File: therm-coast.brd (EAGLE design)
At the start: 44.1 x 36.8 mm, 19 parts, among them U1 ATTINY85-20SU

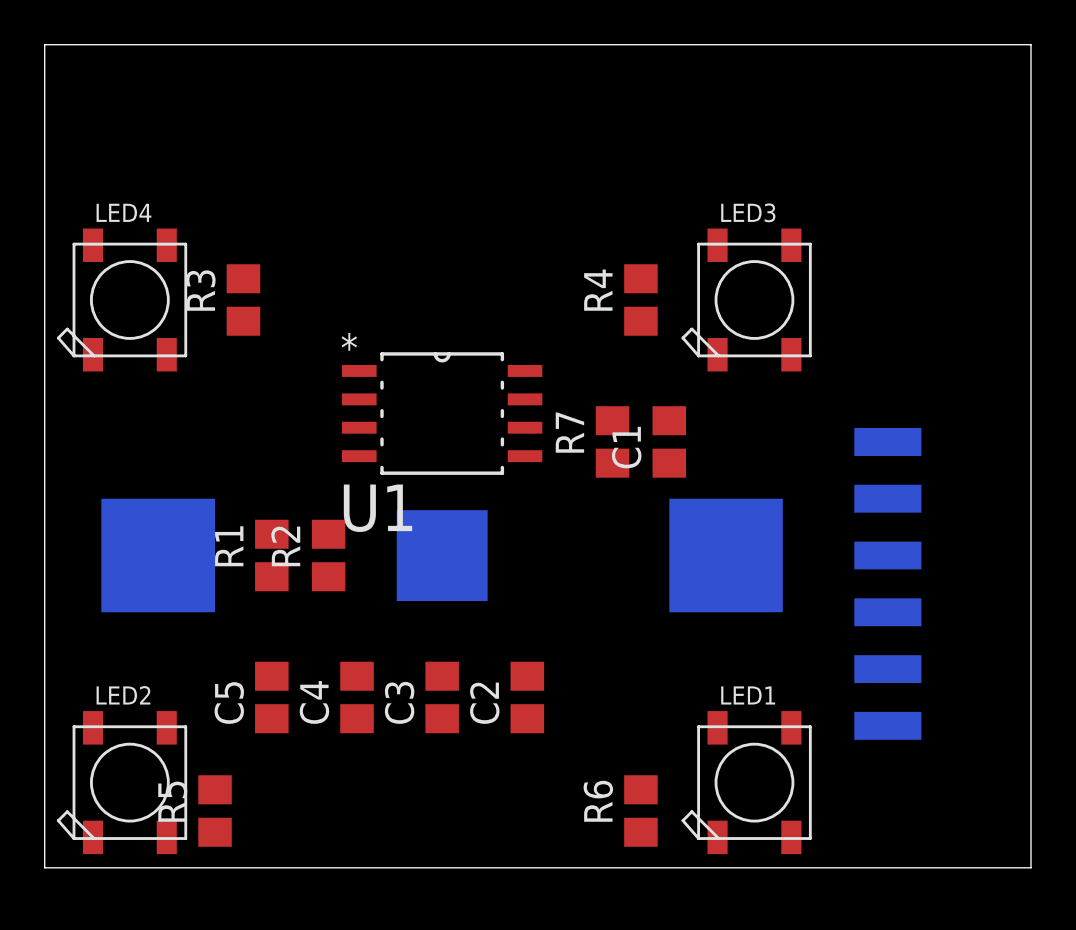
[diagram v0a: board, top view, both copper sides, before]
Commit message: Board Placement and Routing updates
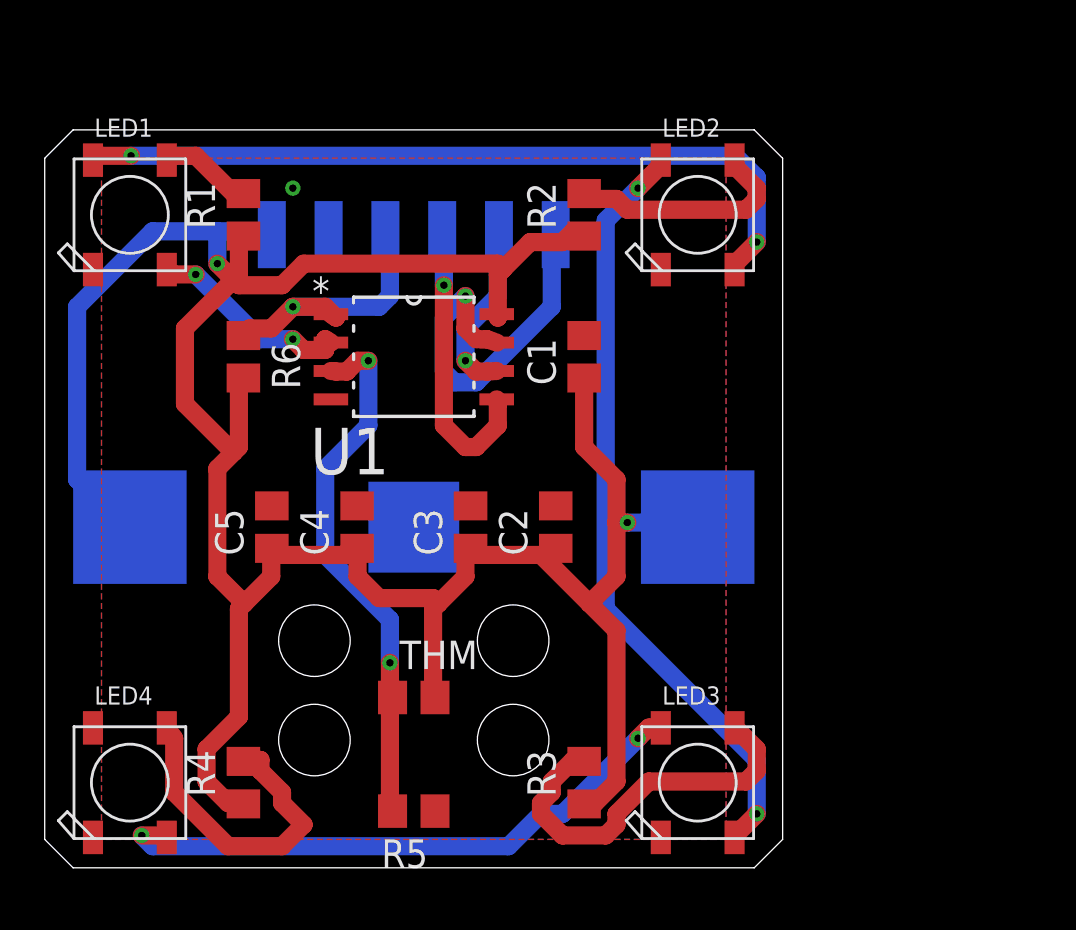
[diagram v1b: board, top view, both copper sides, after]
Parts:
- removed R7: 10K, resistor:R0805
- added THM: 10K, resistor:R0805
- R1, R2: value 10K -> 160
- R5, R6: value 160 -> 10K
- moved LED1 37.8 mm to (3.81, 29.2)
- moved LED2 35.9 mm to (29.2, 29.2)
- moved R4 28.0 mm to (8.89, 3.81)
- moved R6 27.0 mm to (8.89, 22.9), turned to 270 degrees
- moved R3 26.4 mm to (24.1, 3.81)
- moved J1 26.1 mm to (16.5, 31.8), turned to 180 degrees
- moved LED3 21.7 mm to (29.2, 3.81)
- moved LED4 21.6 mm to (3.81, 3.81)
- moved R2 19.1 mm to (24.1, 29.2)
- moved R1 15.3 mm to (8.89, 29.2)
- moved R5 8.89 mm to (16.5, 2.54), turned to 180 degrees
- moved C2 7.73 mm to (22.9, 15.2)
- moved C3 7.73 mm to (19.1, 15.2)
- moved C4 7.62 mm to (14.0, 15.2)
- moved C5 7.62 mm to (10.2, 15.2)
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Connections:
- net GND: now also R5.1; no longer R2.1
- net N$1: now also R1.2; no longer R6.2
- net N$2: now also R2.2; no longer R5.2
- net N$3: now also R3.2; no longer R4.2
- net N$4: now also R4.2; no longer R3.2
- net RESET: now also R6.1; no longer R7.1
- net TEMP: now also R5.2, THM.1; no longer R1.1, R2.2
- net VCC: now also R1.1, R2.1, R6.2, THM.2; no longer R1.2, R5.1, R6.1, R7.2
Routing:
- net VCC: track 0.00 -> 129.6 mm, vias 0 -> 2
- net N$5: track 0.00 -> 34.7 mm, vias 0 -> 2
- net N$6: track 0.00 -> 34.5 mm, vias 0 -> 2
- net N$7: track 0.00 -> 26.8 mm, vias 0 -> 2
- net TEMP: track 0.00 -> 24.1 mm, vias 0 -> 2
- net N$3: track 0.00 -> 17.5 mm
- net SCK/SCL: track 0.00 -> 16.5 mm, vias 0 -> 1
- net N$4: track 0.00 -> 14.6 mm
- net MOSI/SDA: track 0.00 -> 12.9 mm, vias 0 -> 1
- net RESET: track 0.00 -> 12.5 mm, vias 0 -> 1
- net N$2: track 0.00 -> 10.5 mm
- net LED_DATA: track 0.00 -> 9.33 mm, vias 0 -> 2
- net MISO: track 0.00 -> 7.84 mm, vias 0 -> 1
- net N$1: track 0.00 -> 4.39 mm
- added copper zone on layer 1, net GND
- added copper zone on layer 16, net GND
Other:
- board size 44.1 x 36.8 mm -> 33 x 33 mm

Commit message: Rev 1.0
Better Route and Placement, Silks
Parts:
- added LOGO1: OSHW-LOGOL, SparkFun-Aesthetics:OSHW-LOGO-L
- moved R5 8.52 mm to (12.7, 10.2), turned to 270 degrees
- moved J1 5.08 mm to (16.5, 26.7), turned to 0 degrees
- moved THM 4.58 mm to (20.3, 10.2), turned to 270 degrees
- moved C4 2.54 mm to (11.4, 15.2)
- moved C5 2.54 mm to (7.62, 15.2)
- moved C2 2.54 mm to (25.4, 15.2)
- moved C3 2.54 mm to (21.6, 15.2)
- moved U1 2.54 mm to (16.5, 20.3)
- moved BT1 1.27 mm to (16.5, 16.5)
- moved R3 1.27 mm to (24.1, 5.08), turned to 270 degrees
- moved R4 1.27 mm to (8.89, 5.08), turned to 270 degrees
- moved R1 1.27 mm to (8.89, 27.9)
- moved R2 1.27 mm to (24.1, 27.9)
- turned C1 to 0 degrees
- turned R6 to 180 degrees
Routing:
- net VCC: track 129.6 -> 88.9 mm, vias 2 -> 4
- net N$4: track 14.6 -> 4.31 mm
- net N$3: track 17.5 -> 7.61 mm
- net MISO: track 7.84 -> 17.1 mm
- net LED_DATA: track 9.33 -> 12.6 mm, vias 2 -> 0
- net N$5: track 34.7 -> 31.8 mm, vias 2 -> 0
- net N$7: track 26.8 -> 24.3 mm
- net MOSI/SDA: track 12.9 -> 15.2 mm
- net N$2: track 10.5 -> 8.66 mm, vias 0 -> 2
- net N$1: track 4.39 -> 6.14 mm, vias 0 -> 2
- net TEMP: track 24.1 -> 22.4 mm
- net N$6: track 34.5 -> 35.6 mm
- net RESET: track 12.5 -> 13.5 mm
- net SCK/SCL: track 16.5 -> 15.9 mm
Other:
- board text added: "THERM-COASTER Design by: Ray Olsen"

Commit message: Fix #1
Updates to fixz issue with vias exposed to ground plane
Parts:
- moved BT1 3.81 mm to (16.5, 12.7)
- moved U1 2.54 mm to (16.5, 22.9)
- moved C2 1.27 mm to (25.4, 16.5)
- moved C3 1.27 mm to (21.6, 16.5)
- moved C4 1.27 mm to (11.4, 16.5)
- moved C5 1.27 mm to (7.62, 16.5)
- moved C1 1.27 mm to (24.1, 24.1)
- moved R6 1.27 mm to (8.89, 24.1)
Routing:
- net MISO: track 17.1 -> 12.8 mm
- net MOSI/SDA: track 15.2 -> 12.3 mm
- net TEMP: track 22.4 -> 24.9 mm
- net N$1: track 6.14 -> 7.99 mm
- net SCK/SCL: track 15.9 -> 14.1 mm
- net N$5: track 31.8 -> 32.8 mm
- net RESET: track 13.5 -> 12.8 mm
- net VCC: track 88.9 -> 89.4 mm
- net LED_DATA: track 12.6 -> 13.1 mm
